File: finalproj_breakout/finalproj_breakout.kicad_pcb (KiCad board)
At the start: 2 copper layers, 29 parts, among them J1 Conn_02x18_Odd_Even, J2 Conn_02x18_Odd_Even, J3 Conn_02x18_Odd_Even, J4 Conn_02x18_Odd_Even, J8 Programmer_Conn, SW1 RESET_SW, U1 STM32F767ZITx

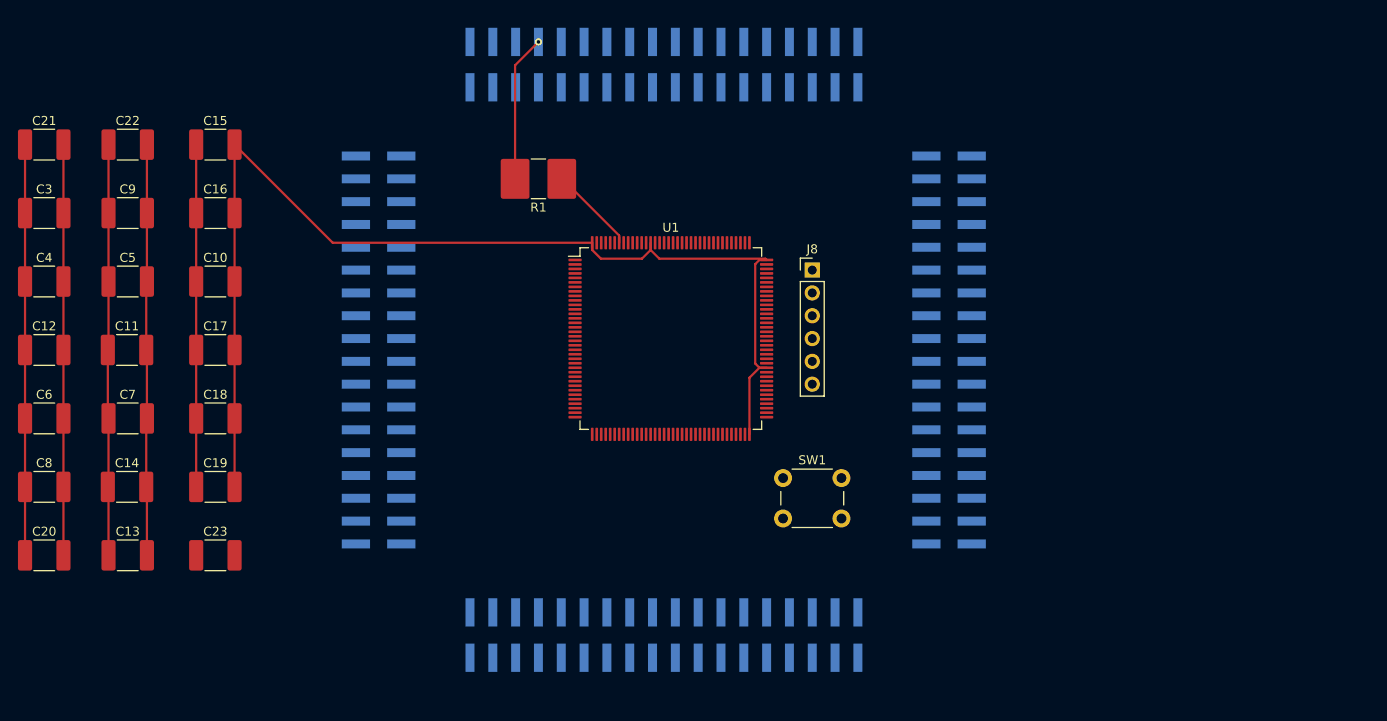
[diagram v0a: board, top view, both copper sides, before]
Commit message: finished a quarter of breakout board connections, placed cap on the back
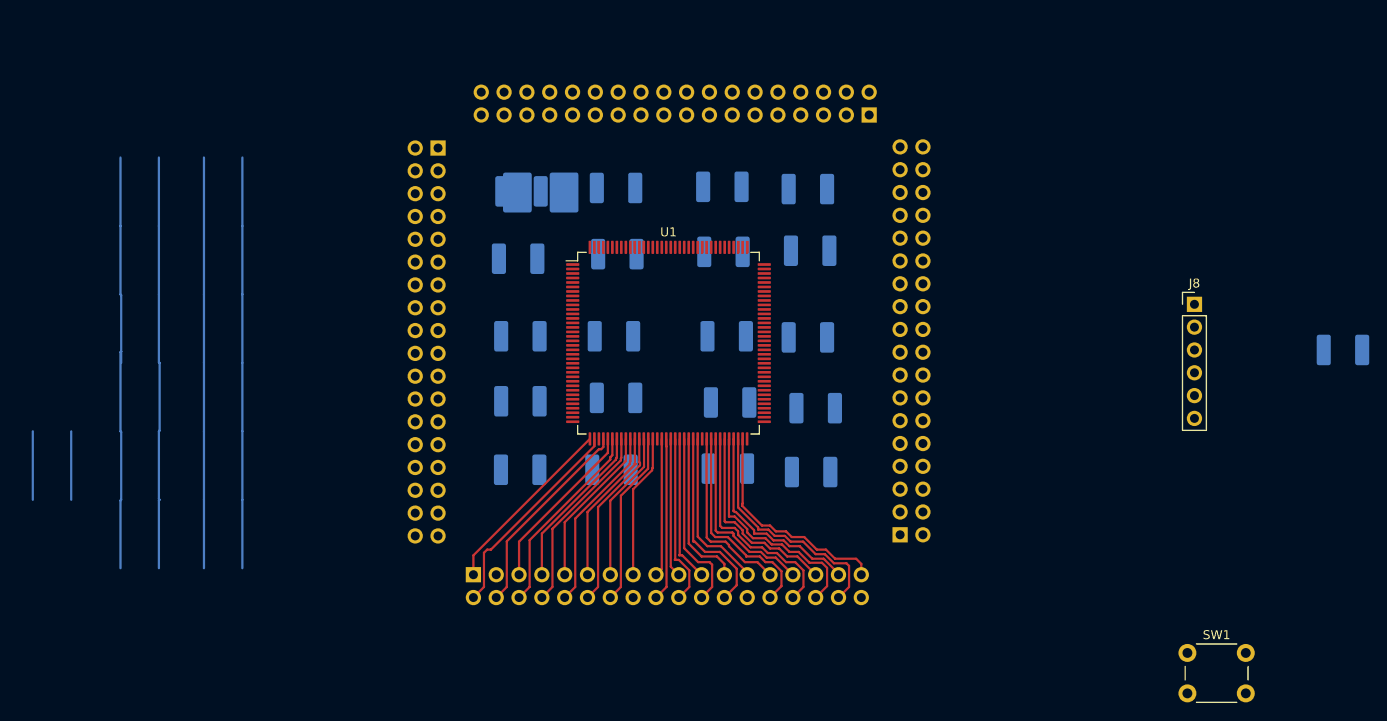
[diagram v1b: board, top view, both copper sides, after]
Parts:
- C10, C11, C12, C13, C14, C15, C16, C17, C18, C19, C20, C21, C22, C23, C3, C4, C5, C6, C7, C8, C9, R1: moved to B.Cu
- J1, J2, J3, J4: footprint Connector_PinHeader_2.54mm:PinHeader_2x18_P2.54mm_Vertical_SMD -> Connector_PinHeader_2.54mm:PinHeader_2x18_P2.54mm_Vertical
- moved C23 127.6 mm to (267.4, 80.0), turned to 180 degrees
- moved C12 86.0 mm to (208.0, 69.0), turned to 180 degrees
- moved C4 85.6 mm to (207.8, 62.1), turned to 180 degrees
- moved C13 78.3 mm to (208.7, 86.5), turned to 180 degrees
- moved C8 77.8 mm to (198.8, 78.5), turned to 180 degrees
- moved C14 77.6 mm to (207.8, 78.6), turned to 180 degrees
- moved C3 75.5 mm to (198.3, 61.8), turned to 180 degrees
- moved C10 69.6 mm to (208.2, 93.6), turned to 180 degrees
- moved C9 66.5 mm to (198.4, 69.1), turned to 180 degrees
- moved C20 66.0 mm to (186.4, 85.3), turned to 180 degrees
- moved C6 64.1 mm to (186.2, 78.5), turned to 180 degrees
- moved C21 63.8 mm to (186.4, 62.0), turned to 180 degrees
- moved C16 61.1 mm to (199.1, 85.9), turned to 180 degrees
- moved J4 58.6 mm to (170.6, 105.0), turned to -90 degrees
- moved C17 58.6 mm to (198.9, 93.2), turned to 180 degrees
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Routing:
- net Net-(J8-VDD_TARGET): track 219.4 -> 100.5 mm
- net VSS: track 129.7 -> 157.0 mm
- net PB11: track 0.00 -> 26.8 mm
- net PE15: track 0.00 -> 26.0 mm
- net PE13: track 0.00 -> 24.7 mm
- net VCAP_1: track 0.00 -> 24.6 mm
- net PE11: track 0.00 -> 23.6 mm
- net PB10: track 0.00 -> 23.0 mm
- net PA4: track 0.00 -> 22.7 mm
- net PE14: track 0.00 -> 22.0 mm
- net PA6: track 0.00 -> 22.0 mm
- net PC4: track 0.00 -> 21.3 mm
- net PE9: track 0.00 -> 21.3 mm
- net PE12: track 0.00 -> 21.0 mm
- net PB0: track 0.00 -> 20.7 mm
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
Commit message: finalized front layer mcu connections, half done with back layer cap connections
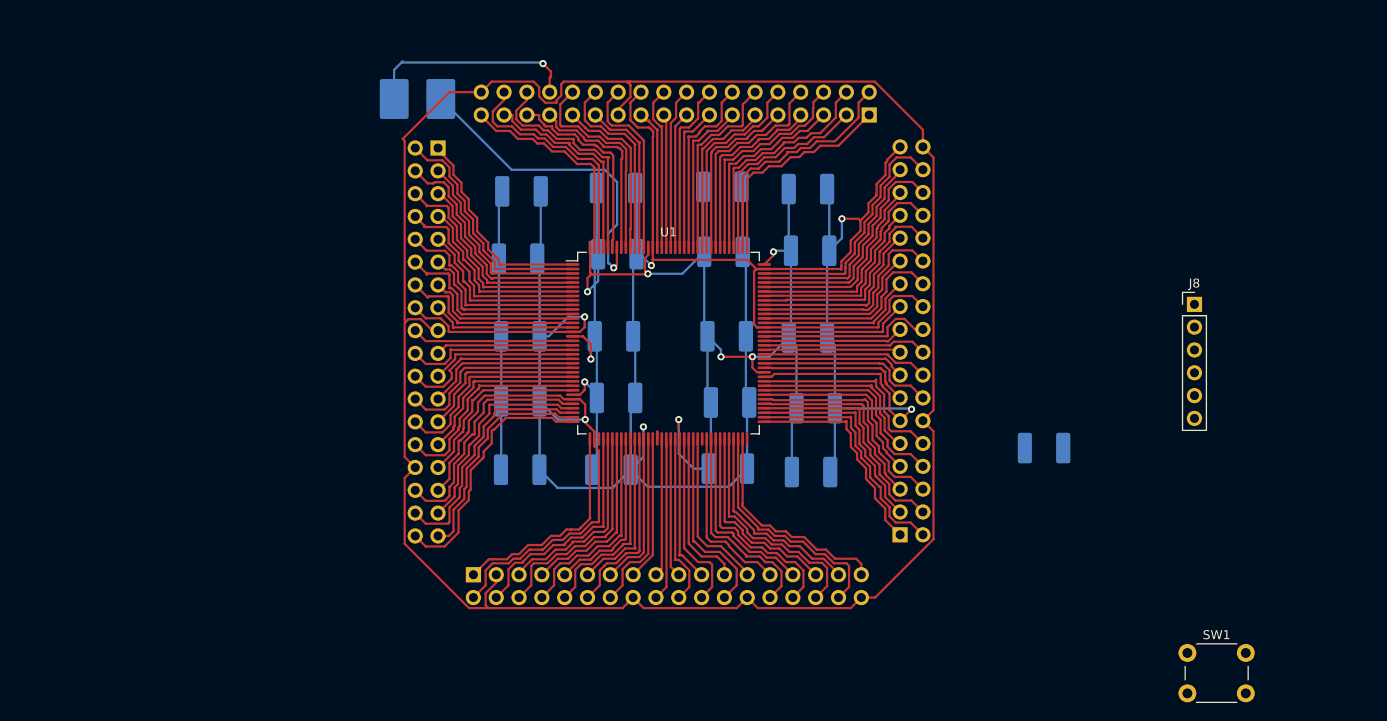
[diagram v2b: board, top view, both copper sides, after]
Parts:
- moved C23 35.0 mm to (234.1, 90.9)
- moved R1 17.2 mm to (164.3, 52.1), turned to 180 degrees
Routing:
- net VSS: track 157.0 -> 430.4 mm, vias 0 -> 6
- net VDD: track 0.00 -> 239.7 mm
- net Net-(J8-VDD_TARGET): track 100.5 -> 194.1 mm, vias 0 -> 8
- net Net-(U1-BOOT0): track 0.00 -> 36.2 mm, vias 0 -> 1
- net PA2: track 0.00 -> 28.6 mm
- net PA0: track 0.00 -> 27.8 mm
- net VCAP_2: track 0.00 -> 27.8 mm
- net PB13: track 0.00 -> 27.2 mm
- net PA15: track 0.00 -> 26.9 mm
- net PE3: track 0.00 -> 26.9 mm
- net VREF+: track 0.00 -> 26.8 mm
- net PE1: track 0.00 -> 26.8 mm
- net PA12: track 0.00 -> 26.4 mm
- net PB15: track 0.00 -> 26.1 mm
- net PB9: track 0.00 -> 26.0 mm
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
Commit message: finished breakout board design
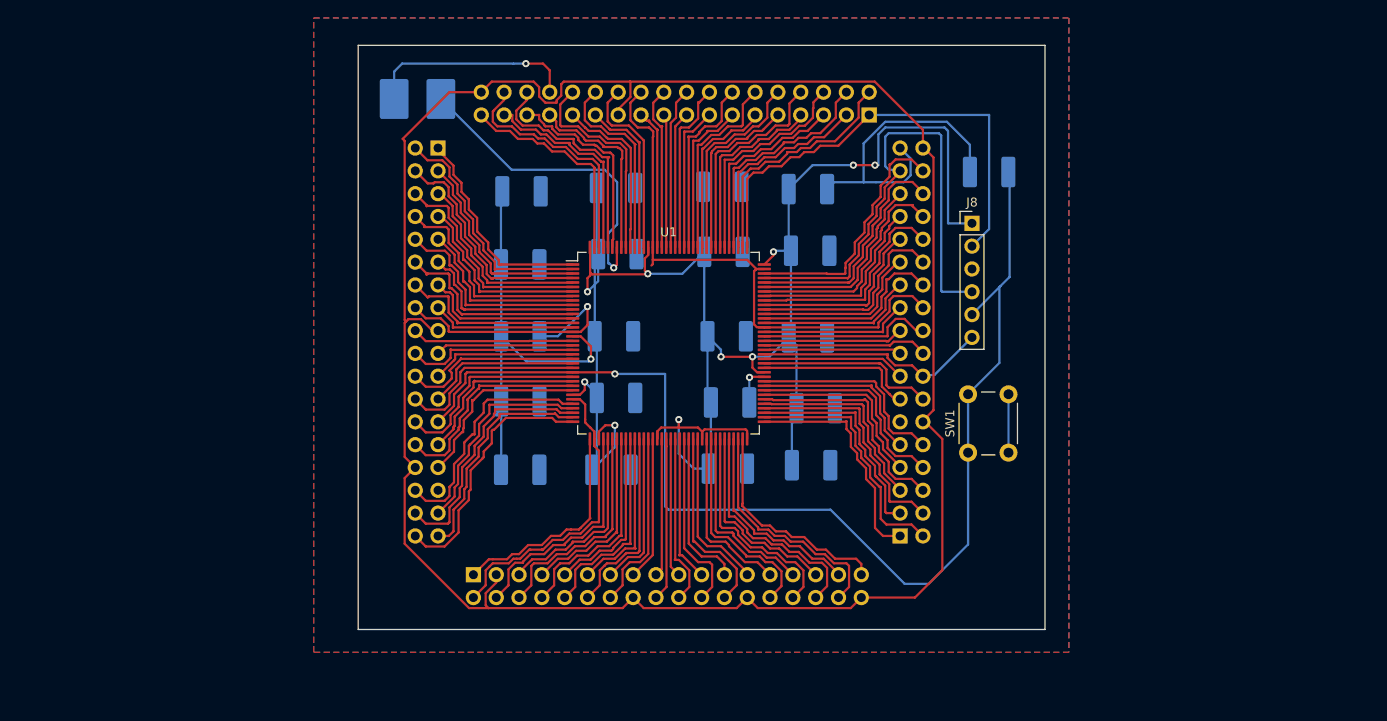
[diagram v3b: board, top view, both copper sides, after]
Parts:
- moved SW1 33.1 mm to (225.6, 91.4), turned to 90 degrees
- moved C23 31.3 mm to (228.0, 60.2)
- moved J8 26.4 mm to (226.1, 65.9)
- moved C10 0.76 mm to (208.2, 92.8)
- moved C11 0.68 mm to (175.8, 70.5)
- moved J3 0.13 mm to (218.1, 100.7)
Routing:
- net VSS: track 430.4 -> 230.1 mm, vias 6 -> 2
- net NRST: track 18.6 -> 130.8 mm, vias 0 -> 1
- net Net-(J8-VDD_TARGET): track 194.1 -> 260.2 mm, vias 8 -> 11
- net PA13: track 23.8 -> 55.9 mm
- net PA14: track 24.1 -> 52.9 mm
- net PG3: track 18.7 -> 26.1 mm
- net VDD: track 239.7 -> 242.7 mm
- net PB12: track 24.3 -> 25.5 mm
- net PB14: track 23.3 -> 24.3 mm
- net PB13: track 27.2 -> 28.0 mm
- net BOOT0: track 24.1 -> 23.5 mm
- added copper zone on B.Cu, net VSS
- added copper zone on F.Cu, net VSS
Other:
- board outline added: 76.5 x 65 mm
